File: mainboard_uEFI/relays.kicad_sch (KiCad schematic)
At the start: 11 parts, among them U10 TPL7407LAPWR, U11 TPL7407LAPWR

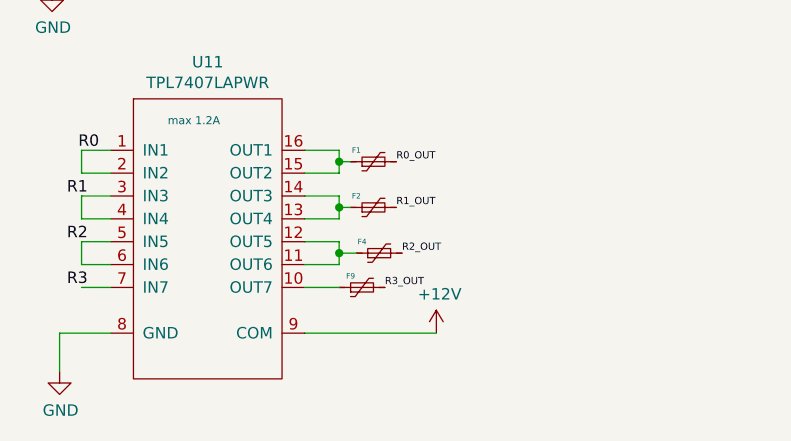
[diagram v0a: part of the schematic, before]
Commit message: uefi v4 mainboard, wip relay
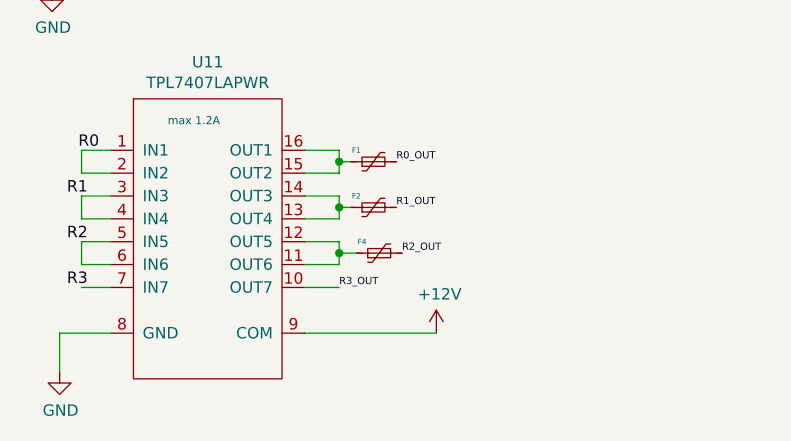
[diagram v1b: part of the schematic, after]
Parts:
- removed F9: 750mA, Fuse:Fuse_1206_3216Metric, symbol Device:Polyfuse_Small
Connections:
- net R3_OUT: now also U11.10 (OUT7)
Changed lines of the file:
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@@
     (effects (font (size 1.27 1.27)) (justify left bottom))
   )
-  (label "R3_OUT" (at 153.67 173.99 0)
+  (label "R3_OUT" (at 148.59 173.99 0)
     (effects (font (size 0.8 0.8)) (justify left bottom))
   )
@@
       (effects (font (size 0.889 0.889)) hide)
     )
-    (pin "1")
-    (pin "2")
-  )
-  (symbol (lib_id "Device:Polyfuse_Small") (at 151.13 173.99 90) (unit 1)
-    (in_bom yes) (on_board yes)
-    (property "Reference" "F9" (id 0) (at 149.86 172.72 90)
-      (effects (font (size 0.6 0.6)))
-    )
-    (property "Value" "750mA" (id 1) (at 156.21 172.085 90)
-      (effects (font (size 1.27 1.27)) hide)
-    )
-    (property "Footprint" "Fuse:Fuse_1206_3216Metric" (id 2) (at 156.21 172.72 0)
-      (effects (font (size 1.27 1.27)) (justify left) hide)
-    )
-    (property "Datasheet" "~" (id 3) (at 151.13 173.99 0)
-      (effects (font (size 1.27 1.27)) hide)
-    )
-    (property "LCSC" "C163130" (id 4) (at 151.13 173.99 90)
-      (effects (font (size 0.889 0.889)) hide)
-    )
